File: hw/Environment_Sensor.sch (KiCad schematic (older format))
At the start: 18 parts, among them P1 CONN_4, U1 MCP1703T, U2 PCA9512ADP, U3 TMP105, U4 HIH-6131-021, U5 MPL115A, U6 TSL2561T

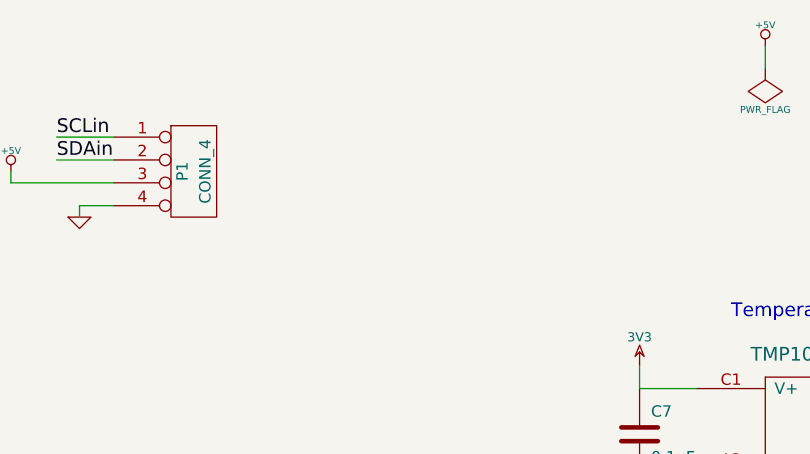
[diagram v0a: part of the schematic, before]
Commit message: Updated v0.02 TSSOP foot print was too big and board looked silly with 4 screw holes.
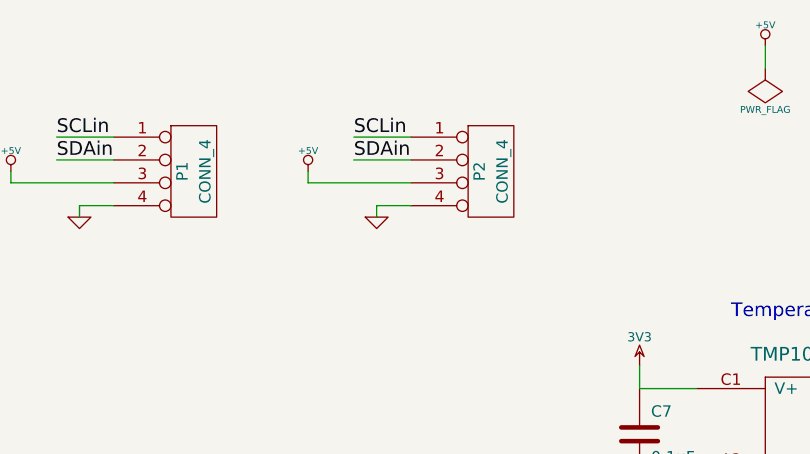
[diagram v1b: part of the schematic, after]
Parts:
- added P2: CONN_4, symbol CONN_4
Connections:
- wire segments 63 -> 69

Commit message: Added a second humidity sensor so you can choose between (£2 vs £12...). Fixed the solder mask padding
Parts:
- added C11: 0.1uF, symbol C
- added U7: HTU21D, symbol HTU21D
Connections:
- wire segments 69 -> 76
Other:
- note added: "Smaller humidity sensor"
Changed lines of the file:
@@
 	5200 1650 5200 1550
 $Comp
-L +5V #PWR18
+L +5V #PWR01
 U 1 1 53729ED8
 P 5200 1550
-F 0 "#PWR18" H 5200 1640 20  0001 C CNN
+F 0 "#PWR01" H 5200 1640 20  0001 C CNN
 F 1 "+5V" H 5200 1640 30  0000 C CNN
 F 2 "" H 5200 1550 60  0001 C CNN
@@
 $EndComp
 $Comp
-L PWR_FLAG #FLG1
+L PWR_FLAG #FLG02
 U 1 1 53729EC8
 P 5200 1650
-F 0 "#FLG1" H 5200 1745 30  0001 C CNN
+F 0 "#FLG02" H 5200 1745 30  0001 C CNN
 F 1 "PWR_FLAG" H 5200 1830 30  0000 C CNN
 F 2 "" H 5200 1650 60  0001 C CNN
@@
 SDA
 $Comp
-L 3V3 #PWR20
+L 3V3 #PWR03
 U 1 1 5372962B
 P 6750 2850
-F 0 "#PWR20" H 6750 2950 40  0001 C CNN
+F 0 "#PWR03" H 6750 2950 40  0001 C CNN
 F 1 "3V3" H 6750 2975 40  0000 C CNN
 F 2 "" H 6750 2850 60  0001 C CNN
@@
 $EndComp
 $Comp
-L GND #PWR19
+L GND #PWR04
 U 1 1 537295E4
 P 6350 3350
-F 0 "#PWR19" H 6350 3350 30  0001 C CNN
+F 0 "#PWR04" H 6350 3350 30  0001 C CNN
 F 1 "GND" H 6350 3280 30  0001 C CNN
 F 2 "" H 6350 3350 60  0001 C CNN
@@
 $EndComp
 $Comp
-L 3V3 #PWR15
+L 3V3 #PWR05
 U 1 1 53729235
 P 4650 2950
-F 0 "#PWR15" H 4650 3050 40  0001 C CNN
+F 0 "#PWR05" H 4650 3050 40  0001 C CNN
 F 1 "3V3" H 4650 3075 40  0000 C CNN
 F 2 "" H 4650 2950 60  0001 C CNN
@@
 $EndComp
 $Comp
-L GND #PWR16
+L GND #PWR06
 U 1 1 5372922C
 P 4650 3500
-F 0 "#PWR16" H 4650 3500 30  0001 C CNN
+F 0 "#PWR06" H 4650 3500 30  0001 C CNN
 F 1 "GND" H 4650 3430 30  0001 C CNN
 F 2 "" H 4650 3500 60  0001 C CNN
@@
 $EndComp
 $Comp
-L GND #PWR17
+L GND #PWR07
 U 1 1 53729228
 P 4850 3450
-F 0 "#PWR17" H 4850 3450 30  0001 C CNN
+F 0 "#PWR07" H 4850 3450 30  0001 C CNN
 F 1 "GND" H 4850 3380 30  0001 C CNN
 F 2 "" H 4850 3450 60  0001 C CNN
@@
 SDA
 $Comp
-L 3V3 #PWR10
+L 3V3 #PWR08
 U 1 1 53728CA5
 P 3450 6700
-F 0 "#PWR10" H 3450 6800 40  0001 C CNN
+F 0 "#PWR08" H 3450 6800 40  0001 C CNN
 F 1 "3V3" H 3450 6825 40  0000 C CNN
 F 2 "" H 3450 6700 60  0001 C CNN
@@
 $EndComp
 $Comp
-L 3V3 #PWR1
+L 3V3 #PWR09
 U 1 1 53728C52
 P 1350 6350
-F 0 "#PWR1" H 1350 6450 40  0001 C CNN
+F 0 "#PWR09" H 1350 6450 40  0001 C CNN
 F 1 "3V3" H 1350 6475 40  0000 C CNN
 F 2 "" H 1350 6350 60  0001 C CNN
@@
 $EndComp
 $Comp
-L GND #PWR13
+L GND #PWR010
 U 1 1 53728C4C
 P 3850 6850
-F 0 "#PWR13" H 3850 6850 30  0001 C CNN
+F 0 "#PWR010" H 3850 6850 30  0001 C CNN
 F 1 "GND" H 3850 6780 30  0001 C CNN
 F 2 "" H 3850 6850 60  0001 C CNN
@@
 $EndComp
 $Comp
-L GND #PWR6
+L GND #PWR011
 U 1 1 53728C0A
 P 2000 6750
-F 0 "#PWR6" H 2000 6750 30  0001 C CNN
+F 0 "#PWR011" H 2000 6750 30  0001 C CNN
 F 1 "GND" H 2000 6680 30  0001 C CNN
 F 2 "" H 2000 6750 60  0001 C CNN
@@
 $EndComp
 $Comp
-L +5V #PWR14
+L +5V #PWR012
 U 1 1 53728BED
 P 3950 6350
-F 0 "#PWR14" H 3950 6440 20  0001 C CNN
+F 0 "#PWR012" H 3950 6440 20  0001 C CNN
 F 1 "+5V" H 3950 6440 30  0000 C CNN
 F 2 "" H 3950 6350 60  0001 C CNN
@@
 $EndComp
 $Comp
-L GND #PWR2
+L GND #PWR013
 U 1 1 53728BD6
 P 1550 6850
-F 0 "#PWR2" H 1550 6850 30  0001 C CNN
+F 0 "#PWR013" H 1550 6850 30  0001 C CNN
 F 1 "GND" H 1550 6780 30  0001 C CNN
 F 2 "" H 1550 6850 60  0001 C CNN
@@
 $EndComp
 $Comp
-L +5V #PWR3
+L +5V #PWR014
 U 1 1 537288EE
 P 1700 3850
-F 0 "#PWR3" H 1700 3940 20  0001 C CNN
+F 0 "#PWR014" H 1700 3940 20  0001 C CNN
 F 1 "+5V" H 1700 3940 30  0000 C CNN
 F 2 "" H 1700 3850 60  0001 C CNN
@@
 $EndComp
 $Comp
-L 3V3 #PWR12
+L 3V3 #PWR015
 U 1 1 537288E9
 P 3500 3900
-F 0 "#PWR12" H 3500 4000 40  0001 C CNN
+F 0 "#PWR015" H 3500 4000 40  0001 C CNN
 F 1 "3V3" H 3500 4025 40  0000 C CNN
 F 2 "" H 3500 3900 60  0001 C CNN
@@
 $EndComp
 $Comp
-L GND #PWR5
+L GND #PWR016
 U 1 1 537288DE
 P 1950 4350
-F 0 "#PWR5" H 1950 4350 30  0001 C CNN
+F 0 "#PWR016" H 1950 4350 30  0001 C CNN
 F 1 "GND" H 1950 4280 30  0001 C CNN
 F 2 "" H 1950 4350 60  0001 C CNN
@@
 $EndComp
 $Comp
-L GND #PWR8
+L GND #PWR017
 U 1 1 537288D9
 P 2600 4550
-F 0 "#PWR8" H 2600 4550 30  0001 C CNN
+F 0 "#PWR017" H 2600 4550 30  0001 C CNN
 F 1 "GND" H 2600 4480 30  0001 C CNN
 F 2 "" H 2600 4550 60  0001 C CNN
@@
 $EndComp
 $Comp
-L 3V3 #PWR26
+L 3V3 #PWR018
 U 1 1 5372789B
 P 8150 5300
-F 0 "#PWR26" H 8150 5400 40  0001 C CNN
+F 0 "#PWR018" H 8150 5400 40  0001 C CNN
 F 1 "3V3" H 8150 5425 40  0000 C CNN
 F 2 "" H 8150 5300 60  0001 C CNN
@@
 $EndComp
 $Comp
-L 3V3 #PWR23
+L 3V3 #PWR019
 U 1 1 53727880
 P 7550 4500
-F 0 "#PWR23" H 7550 4600 40  0001 C CNN
+F 0 "#PWR019" H 7550 4600 40  0001 C CNN
 F 1 "3V3" H 7550 4625 40  0000 C CNN
 F 2 "" H 7550 4500 60  0001 C CNN
@@
 $EndComp
 $Comp
-L GND #PWR24
+L GND #PWR020
 U 1 1 5372787B
 P 7550 5200
-F 0 "#PWR24" H 7550 5200 30  0001 C CNN
+F 0 "#PWR020" H 7550 5200 30  0001 C CNN
 F 1 "GND" H 7550 5130 30  0001 C CNN
 F 2 "" H 7550 5200 60  0001 C CNN
@@
 NoConn ~ 9700 5100
 $Comp
-L GND #PWR22
+L GND #PWR021
 U 1 1 537277D0
 P 7400 3500
-F 0 "#PWR22" H 7400 3500 30  0001 C CNN
+F 0 "#PWR021" H 7400 3500 30  0001 C CNN
 F 1 "GND" H 7400 3430 30  0001 C CNN
 F 2 "" H 7400 3500 60  0001 C CNN
@@
 $EndComp
 $Comp
-L 3V3 #PWR21
+L 3V3 #PWR022
 U 1 1 537277C9
 P 7400 2800
-F 0 "#PWR21" H 7400 2900 40  0001 C CNN
+F 0 "#PWR022" H 7400 2900 40  0001 C CNN
 F 1 "3V3" H 7400 2925 40  0000 C CNN
 F 2 "" H 7400 2800 60  0001 C CNN
@@
 $EndComp
 $Comp
-L 3V3 #PWR25
+L 3V3 #PWR023
 U 1 1 53727546
 P 7800 6150
-F 0 "#PWR25" H 7800 6250 40  0001 C CNN
+F 0 "#PWR023" H 7800 6250 40  0001 C CNN
 F 1 "3V3" H 7800 6275 40  0000 C CNN
 F 2 "" H 7800 6150 60  0001 C CNN
@@
 $EndComp
 $Comp
-L GND #PWR27
+L GND #PWR024
 U 1 1 5372753A
 P 8300 6600
-F 0 "#PWR27" H 8300 6600 30  0001 C CNN
+F 0 "#PWR024" H 8300 6600 30  0001 C CNN
 F 1 "GND" H 8300 6530 30  0001 C CNN
 F 2 "" H 8300 6600 60  0001 C CNN
@@
 $EndComp
 $Comp
-L +5V #PWR4
+L +5V #PWR025
 U 1 1 53726FA2
 P 1900 2100
-F 0 "#PWR4" H 1900 2190 20  0001 C CNN
+F 0 "#PWR025" H 1900 2190 20  0001 C CNN
 F 1 "+5V" H 1900 2190 30  0000 C CNN
 F 2 "" H 1900 2100 60  0001 C CNN
@@
 $EndComp
 $Comp
-L GND #PWR7
+L GND #PWR026
 U 1 1 53726F75
 P 2200 2300
-F 0 "#PWR7" H 2200 2300 30  0001 C CNN
+F 0 "#PWR026" H 2200 2300 30  0001 C CNN
 F 1 "GND" H 2200 2230 30  0001 C CNN
 F 2 "" H 2200 2300 60  0001 C CNN
@@
 	3200 2150 3200 2100
 $Comp
-L +5V #PWR9
+L +5V #PWR027
 U 1 1 539395D4
 P 3200 2100
-F 0 "#PWR9" H 3200 2190 20  0001 C CNN
+F 0 "#PWR027" H 3200 2190 20  0001 C CNN
 F 1 "+5V" H 3200 2190 30  0000 C CNN
 F 2 "" H 3200 2100 60  0001 C CNN
@@
 $EndComp
 $Comp
-L GND #PWR11
+L GND #PWR028
 U 1 1 539395DA
 P 3500 2300
-F 0 "#PWR11" H 3500 2300 30  0001 C CNN
+F 0 "#PWR028" H 3500 2300 30  0001 C CNN
 F 1 "GND" H 3500 2230 30  0001 C CNN
 F 2 "" H 3500 2300 60  0001 C CNN
@@
 	1    0    0    -1
 $EndComp
+$Comp
+L HTU21D U7
+U 1 1 53BB0FF3
+P 8800 1450
+F 0 "U7" H 9000 1000 60  0000 C CNN
+F 1 "HTU21D" H 8750 1600 60  0000 C CNN
+F 2 "" H 8750 1450 60  0000 C CNN
+F 3 "" H 8750 1450 60  0000 C CNN
+	1    8800 1450
+	1    0    0    -1
+$EndComp
+Wire Wire Line
+	9350 1400 9700 1400
+Wire Wire Line
+	9350 1500 9700 1500
+Wire Wire Line
+	8250 1400 8100 1400
+Wire Wire Line
+	8100 1400 8100 1350
+$Comp
+L C C11
+U 1 1 53BB114E
+P 8100 1600
+F 0 "C11" H 8100 1700 40  0000 L CNN
+F 1 "0.1uF" H 7900 1500 40  0000 L CNN
+F 2 "" H 8138 1450 30  0000 C CNN
+F 3 "" H 8100 1600 60  0000 C CNN
+	1    8100 1600
+	1    0    0    -1
+$EndComp
+Wire Wire Line
+	8250 1800 8100 1800
+Wire Wire Line
+	8250 1650 8250 1800
+Wire Wire Line
+	8100 1800 8100 1900
+$Comp
+L GND #PWR029
+U 1 1 53BB120C
+P 8100 1900
+F 0 "#PWR029" H 8100 1900 30  0001 C CNN
+F 1 "GND" H 8100 1830 30  0001 C CNN
+F 2 "" H 8100 1900 60  0000 C CNN
+F 3 "" H 8100 1900 60  0000 C CNN
+	1    8100 1900
+	1    0    0    -1
+$EndComp
+$Comp
+L 3V3 #PWR030
+U 1 1 53BB122F
+P 8100 1350
+F 0 "#PWR030" H 8100 1450 40  0001 C CNN
+F 1 "3V3" H 8100 1475 40  0000 C CNN
+F 2 "" H 8100 1350 60  0000 C CNN
+F 3 "" H 8100 1350 60  0000 C CNN
+	1    8100 1350
+	1    0    0    -1
+$EndComp
+Text Label 9450 1400 0    60   ~ 0
+SCL
+Text Label 9450 1500 0    60   ~ 0
+SDA
+Text Notes 8300 1150 0    60   ~ 0
+Smaller humidity sensor
+Connection ~ 8250 1750
 $EndSCHEMATC

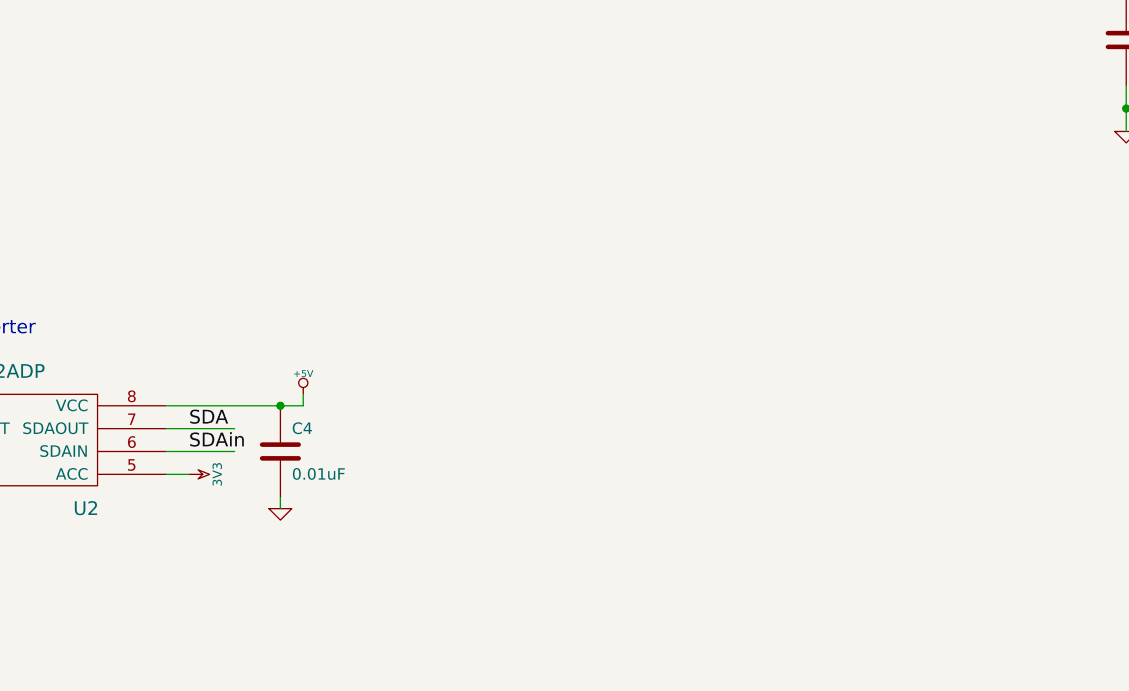
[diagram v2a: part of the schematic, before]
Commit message: Added missed passives on the I2C level converter
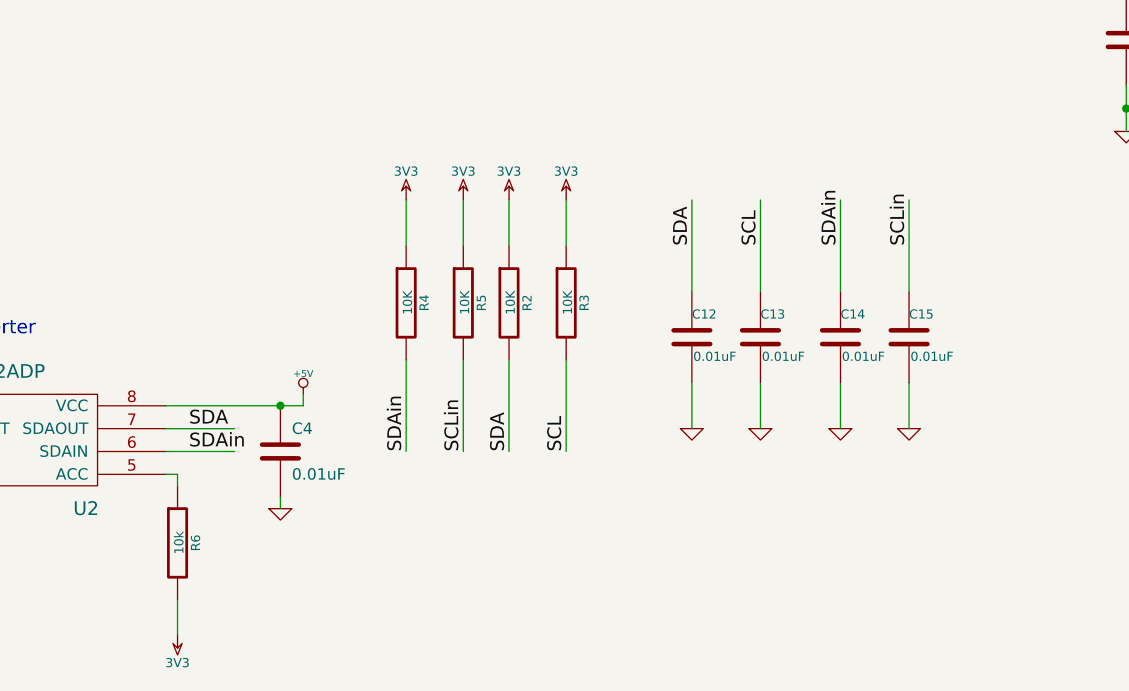
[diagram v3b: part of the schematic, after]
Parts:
- added C12, C13, C14, C15: 0.01uF, symbol C
- added R2, R3, R4, R5: 10K, symbol R
- added R6: 10k, symbol R
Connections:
- wire segments 76 -> 94
